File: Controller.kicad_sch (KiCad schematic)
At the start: 1 part

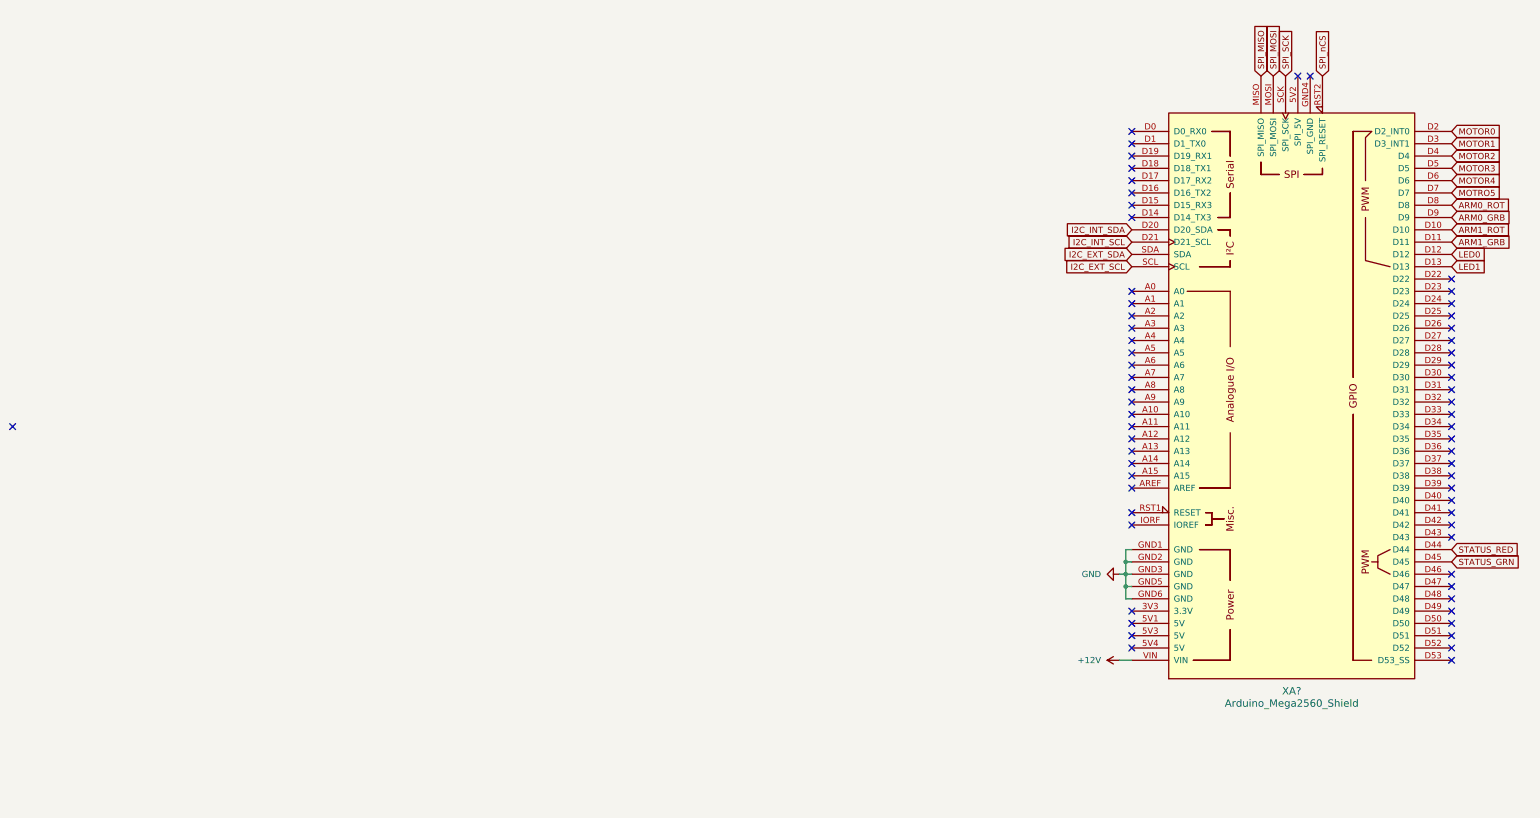
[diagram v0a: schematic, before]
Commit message: Add power supplies & filters
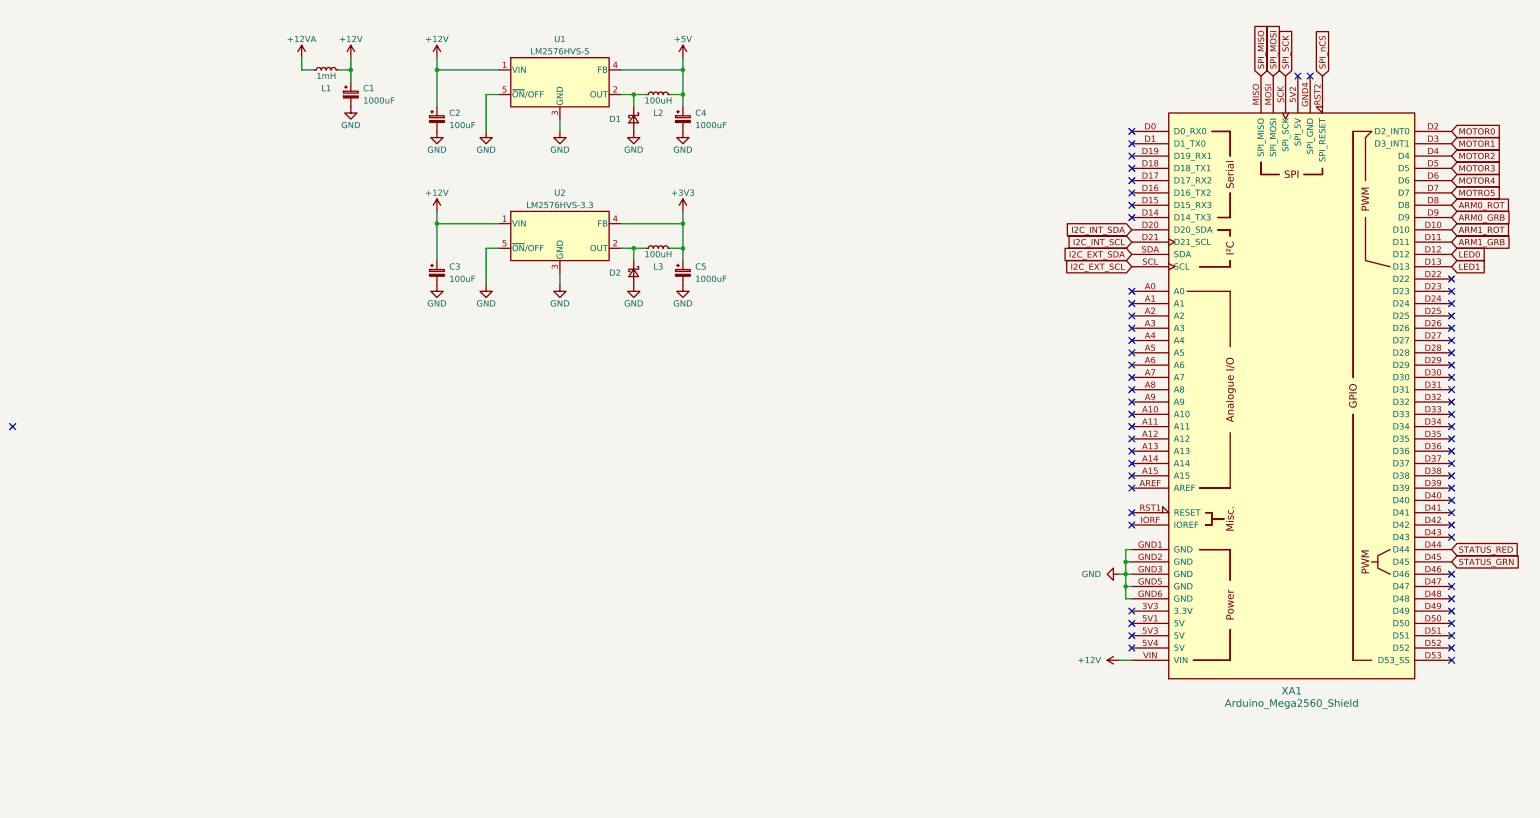
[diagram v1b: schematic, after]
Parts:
- added C1, C4, C5: 1000uF, Capacitor_THT:CP_Radial_D12.5mm_P5.00mm, symbol Device:C_Polarized_Small
- added C2, C3: 100uF, Capacitor_SMD:CP_Elec_6.3x5.9, symbol Device:C_Polarized_Small
- added D1, D2: ~, Diode_SMD:D_SMC, symbol Device:D_Schottky_Small
- added L1: 1mH, Inductor_THT:L_Radial_D24.4mm_P23.40mm_Murata_1400series, symbol Device:L_Small
- added L2, L3: 100uH, Inductor_SMD:L_Bourns_SRR1210A, symbol Device:L_Small
- added U1: LM2576HVS-5, Package_TO_SOT_SMD:TO-263-5_TabPin3, symbol Regulator_Switching:LM2576HVS-5
- added U2: LM2576HVS-3.3, Package_TO_SOT_SMD:TO-263-5_TabPin3, symbol Regulator_Switching:LM2576HVS-3.3
- gave numbers to parts that had none: 1
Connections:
- net +12V: now also C1.1, C2.1, C3.1, L1.2, U1.1 (VIN), U2.1 (VIN)
- net GND: now also C1.2, C2.2, C3.2, C4.2, C5.2, D1.2 (A), D2.2 (A), U1.3 (GND), U1.5 (~{ON}/OFF), U2.3 (GND), U2.5 (~{ON}/OFF)
- new net: D1.1 (K), L2.1, U1.2 (OUT)
- new net: D2.1 (K), L3.1, U2.2 (OUT)
- new net +12VA: L1.1
- new net +3V3: C5.1, L3.2, U2.4 (FB)
- new net +5V: C4.1, L2.2, U1.4 (FB)

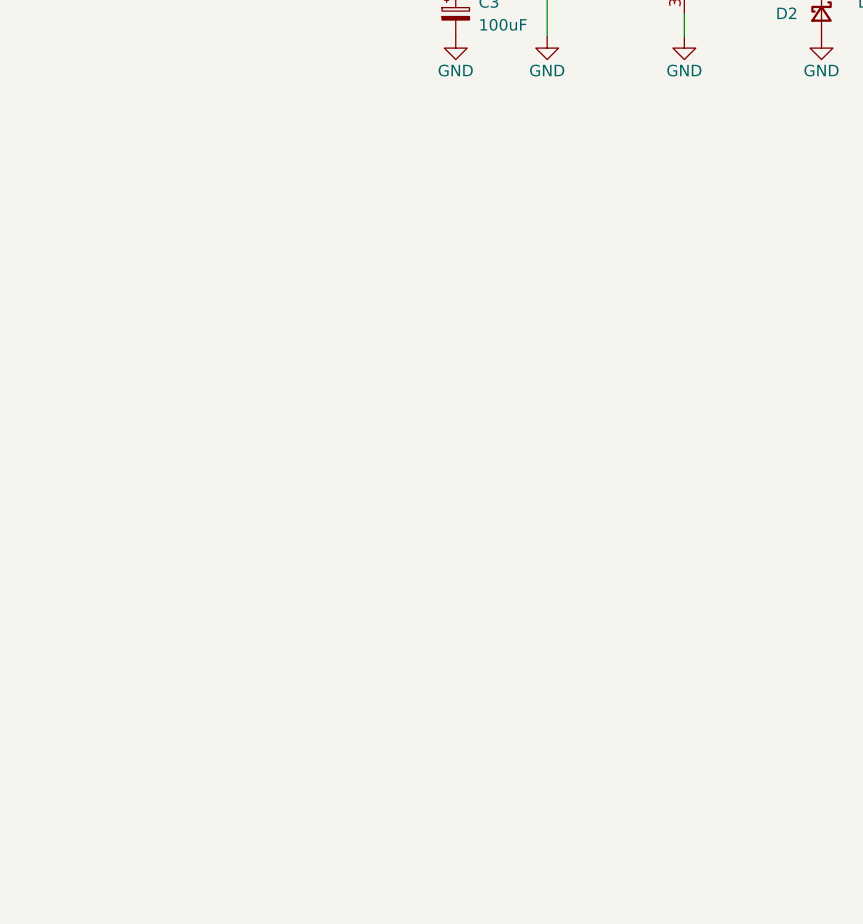
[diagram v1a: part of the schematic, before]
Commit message: Add motor connectors
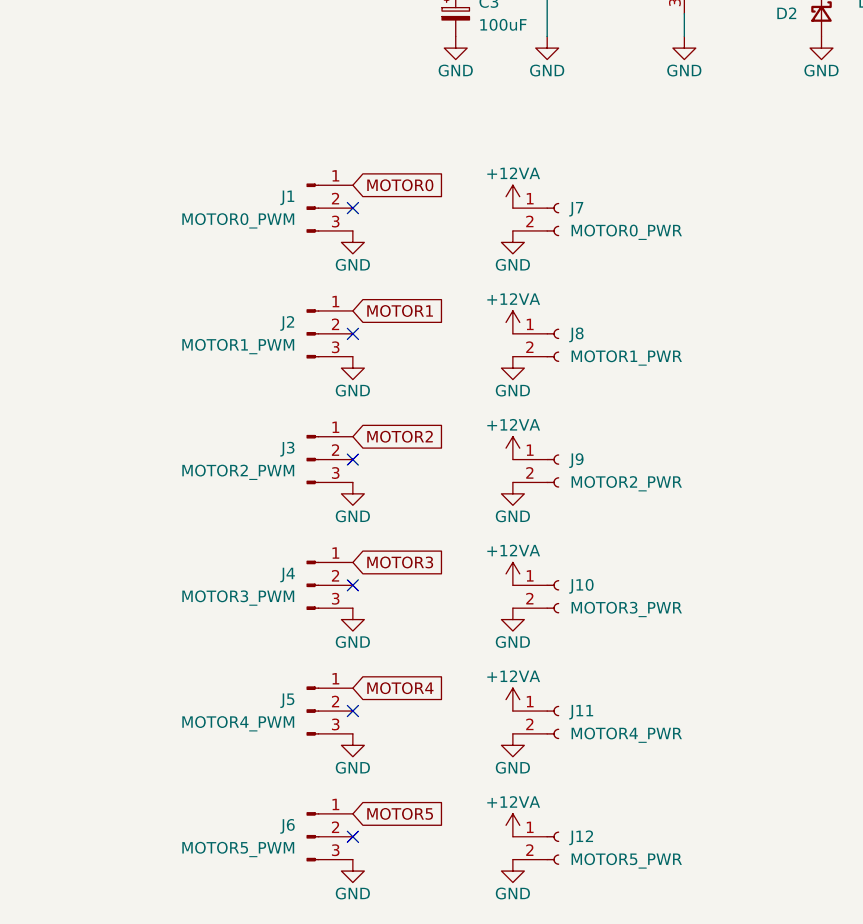
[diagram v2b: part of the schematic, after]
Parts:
- added J1: MOTOR0_PWM, Connector_PinHeader_2.54mm:PinHeader_1x03_P2.54mm_Horizontal, symbol Connector:Conn_01x03_Male
- added J10: MOTOR3_PWR, Controller:ESC-PWR, symbol Connector:Conn_01x02_Female
- added J11: MOTOR4_PWR, Controller:ESC-PWR, symbol Connector:Conn_01x02_Female
- added J12: MOTOR5_PWR, Controller:ESC-PWR, symbol Connector:Conn_01x02_Female
- added J2: MOTOR1_PWM, Connector_PinHeader_2.54mm:PinHeader_1x03_P2.54mm_Horizontal, symbol Connector:Conn_01x03_Male
- added J3: MOTOR2_PWM, Connector_PinHeader_2.54mm:PinHeader_1x03_P2.54mm_Horizontal, symbol Connector:Conn_01x03_Male
- added J4: MOTOR3_PWM, Connector_PinHeader_2.54mm:PinHeader_1x03_P2.54mm_Horizontal, symbol Connector:Conn_01x03_Male
- added J5: MOTOR4_PWM, Connector_PinHeader_2.54mm:PinHeader_1x03_P2.54mm_Horizontal, symbol Connector:Conn_01x03_Male
- added J6: MOTOR5_PWM, Connector_PinHeader_2.54mm:PinHeader_1x03_P2.54mm_Horizontal, symbol Connector:Conn_01x03_Male
- added J7: MOTOR0_PWR, Controller:ESC-PWR, symbol Connector:Conn_01x02_Female
- added J8: MOTOR1_PWR, Controller:ESC-PWR, symbol Connector:Conn_01x02_Female
- added J9: MOTOR2_PWR, Controller:ESC-PWR, symbol Connector:Conn_01x02_Female
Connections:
- net +12VA: now also J10.1 (Pin_1), J11.1 (Pin_1), J12.1 (Pin_1), J7.1 (Pin_1), J8.1 (Pin_1), J9.1 (Pin_1)
- net GND: now also J1.3 (Pin_3), J10.2 (Pin_2), J11.2 (Pin_2), J12.2 (Pin_2), J2.3 (Pin_3), J3.3 (Pin_3), J4.3 (Pin_3), J5.3 (Pin_3), J6.3 (Pin_3), J7.2 (Pin_2), J8.2 (Pin_2), J9.2 (Pin_2)
- net MOTOR0: now also J1.1 (Pin_1)
- net MOTOR1: now also J2.1 (Pin_1)
- net MOTOR2: now also J3.1 (Pin_1)
- net MOTOR3: now also J4.1 (Pin_1)
- net MOTOR4: now also J5.1 (Pin_1)
- new net MOTOR5: J6.1 (Pin_1)
- no-connect marks 64 -> 70

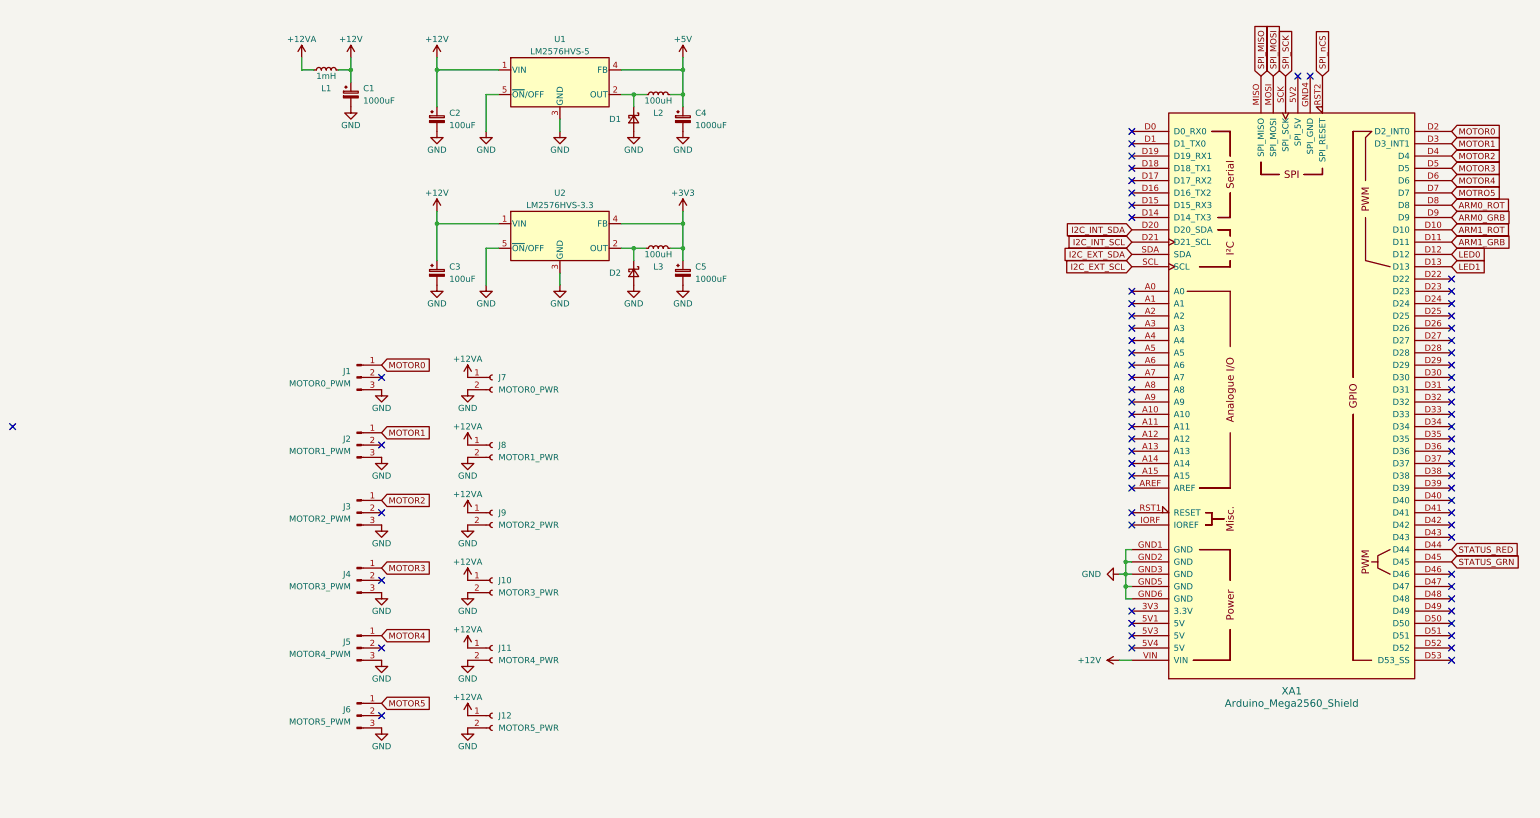
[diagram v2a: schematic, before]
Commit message: Add peripheral connectors
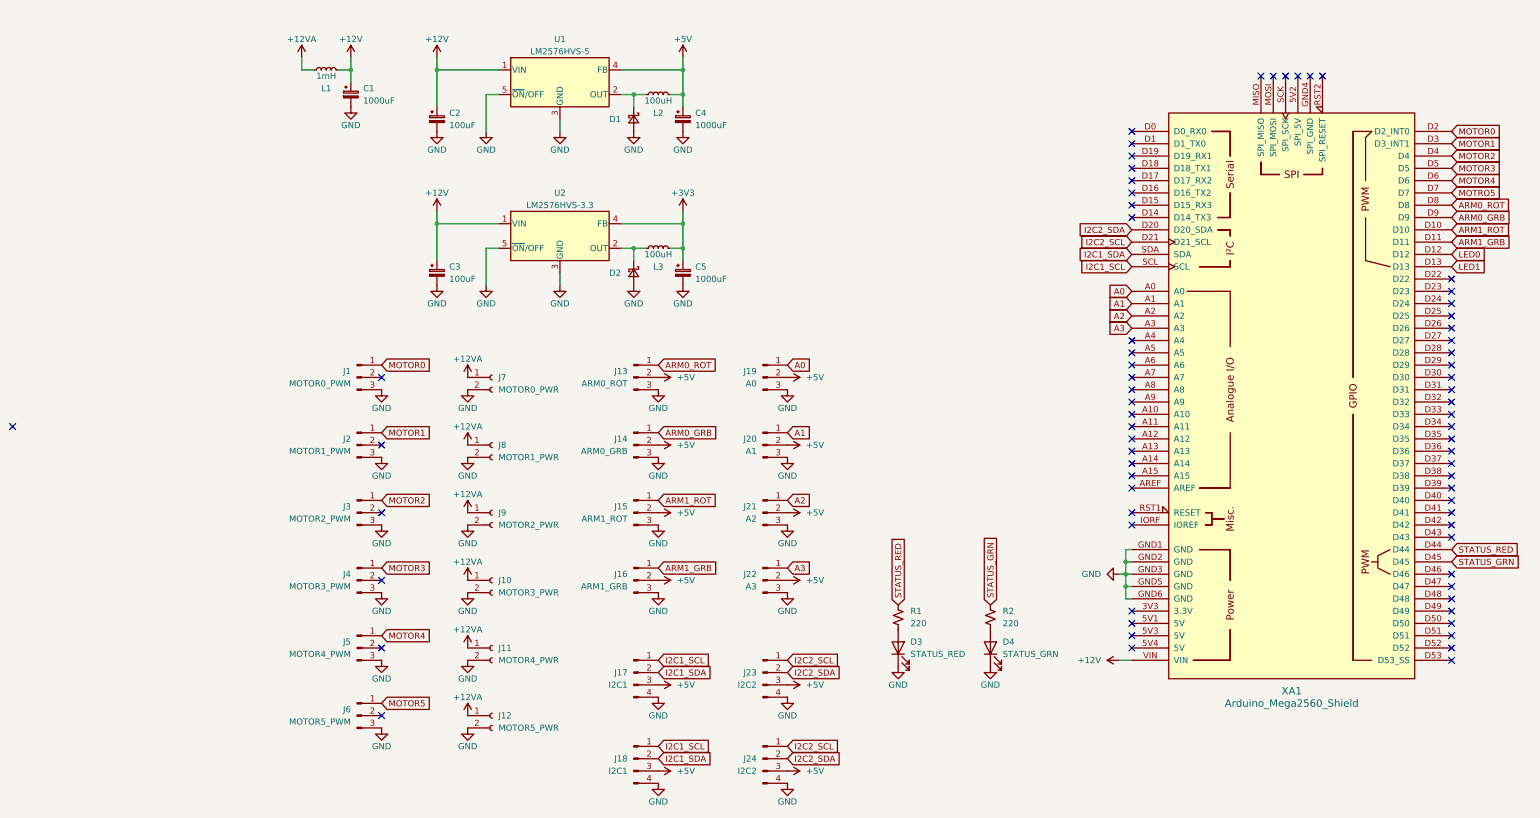
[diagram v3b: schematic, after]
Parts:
- added D3: STATUS_RED, Diode_SMD:D_0402_1005Metric, symbol Device:LED
- added D4: STATUS_GRN, Diode_SMD:D_0402_1005Metric, symbol Device:LED
- added J13: ARM0_ROT, Connector_PinHeader_2.54mm:PinHeader_1x03_P2.54mm_Vertical, symbol Connector:Conn_01x03_Male
- added J14: ARM0_GRB, Connector_PinHeader_2.54mm:PinHeader_1x03_P2.54mm_Vertical, symbol Connector:Conn_01x03_Male
- added J15: ARM1_ROT, Connector_PinHeader_2.54mm:PinHeader_1x03_P2.54mm_Vertical, symbol Connector:Conn_01x03_Male
- added J16: ARM1_GRB, Connector_PinHeader_2.54mm:PinHeader_1x03_P2.54mm_Vertical, symbol Connector:Conn_01x03_Male
- added J17, J18: I2C1, Connector_PinHeader_2.54mm:PinHeader_1x04_P2.54mm_Vertical, symbol Connector:Conn_01x04_Male
- added J19: A0, Connector_PinHeader_2.54mm:PinHeader_1x03_P2.54mm_Vertical, symbol Connector:Conn_01x03_Male
- added J20: A1, Connector_PinHeader_2.54mm:PinHeader_1x03_P2.54mm_Vertical, symbol Connector:Conn_01x03_Male
- added J21: A2, Connector_PinHeader_2.54mm:PinHeader_1x03_P2.54mm_Vertical, symbol Connector:Conn_01x03_Male
- added J22: A3, Connector_PinHeader_2.54mm:PinHeader_1x03_P2.54mm_Vertical, symbol Connector:Conn_01x03_Male
- added J23, J24: I2C2, Connector_PinHeader_2.54mm:PinHeader_1x04_P2.54mm_Vertical, symbol Connector:Conn_01x04_Male
- added R1, R2: 220, Resistor_SMD:R_0402_1005Metric, symbol Device:R_Small_US
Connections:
- net +5V: now also J13.2 (Pin_2), J14.2 (Pin_2), J15.2 (Pin_2), J16.2 (Pin_2), J17.3 (Pin_3), J18.3 (Pin_3), J19.2 (Pin_2), J20.2 (Pin_2), J21.2 (Pin_2), J22.2 (Pin_2), J23.3 (Pin_3), J24.3 (Pin_3)
- net ARM0_GRB: now also J14.1 (Pin_1)
- net ARM0_ROT: now also J13.1 (Pin_1)
- net ARM1_GRB: now also J16.1 (Pin_1)
- net ARM1_ROT: now also J15.1 (Pin_1)
- net GND: now also D3.1 (K), D4.1 (K), J13.3 (Pin_3), J14.3 (Pin_3), J15.3 (Pin_3), J16.3 (Pin_3), J17.4 (Pin_4), J18.4 (Pin_4), J19.3 (Pin_3), J20.3 (Pin_3), J21.3 (Pin_3), J22.3 (Pin_3), J23.4 (Pin_4), J24.4 (Pin_4)
- net STATUS_GRN: now also R2.1
- net STATUS_RED: now also R1.1
- net A0: now reaches XA1.A0
- net A0: now also J19.1 (Pin_1)
- net A1: now reaches XA1.A1
- net A1: now also J20.1 (Pin_1)
- net A2: now reaches XA1.A2
- net A2: now also J21.1 (Pin_1)
- net A3: now reaches XA1.A3
- net A3: now also J22.1 (Pin_1)
- net I2C_EXT_SCL renamed I2C1_SCL
- net I2C1_SCL: now also J17.1 (Pin_1), J18.1 (Pin_1)
- net I2C_EXT_SDA renamed I2C1_SDA
- net I2C1_SDA: now also J17.2 (Pin_2), J18.2 (Pin_2)
- net I2C_INT_SCL renamed I2C2_SCL
- net I2C2_SCL: now also J23.1 (Pin_1), J24.1 (Pin_1)
- net I2C_INT_SDA renamed I2C2_SDA
- net I2C2_SDA: now also J23.2 (Pin_2), J24.2 (Pin_2)
- net SPI_MISO: no longer names the net of XA1.MISO (SPI_MISO)
- net SPI_MOSI: no longer names the net of XA1.MOSI (SPI_MOSI)
- net SPI_SCK: no longer names the net of XA1.SCK (SPI_SCK)
- net SPI_nCS: no longer names the net of XA1.RST2 (SPI_RESET)
- new net: D3.2 (A), R1.2
- new net: D4.2 (A), R2.2
